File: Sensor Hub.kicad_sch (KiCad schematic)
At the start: 37 parts, among them J1 SWD, J2 SD_Card, J4 USB_B_Micro, SW1 SW_SPDT, SW2 SW_Push, U1 LM20BIM7, U2 STM32L100RBT6A_LQFP64, U3 LD_SSOP, U5 AM2320, U7 APDS-9960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

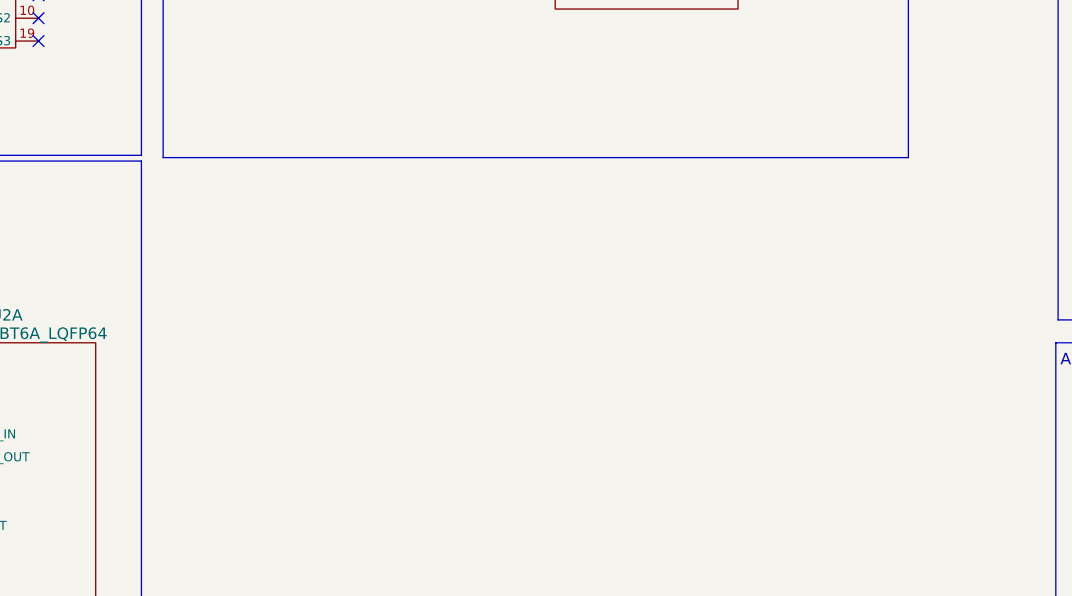
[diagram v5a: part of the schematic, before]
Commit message: Updated Rev 2.0
+ Revamped board to 4 layer with components on both signal layers (top/bottom)
+ Adjusted compactness of components, reducing size by approx 30%
+ Added mounting holes for mounting purposes
- Removed battery, batt charger, eFuse (USB driven only)
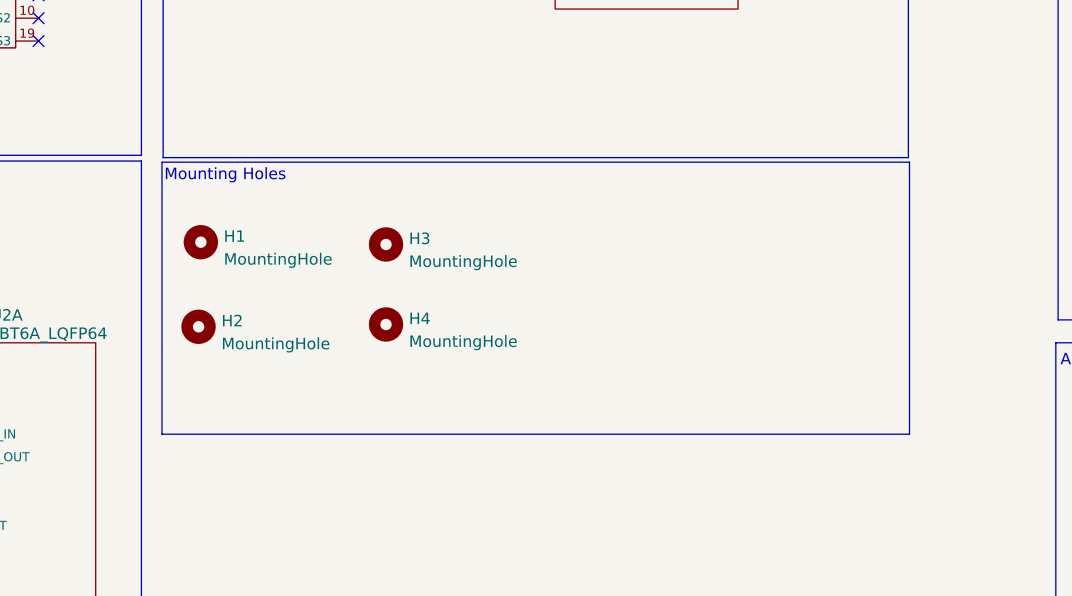
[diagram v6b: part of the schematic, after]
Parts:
- added H1, H2, H3, H4: MountingHole, MountingHole:MountingHole_2.5mm_Pad_Via, symbol Mechanical:MountingHole
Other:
- note added: "Mounting Holes"
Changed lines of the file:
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@@
     (title "Sensor Hub")
     (date "2023-04-03")
-    (rev "1.1")
+    (rev "2.0")
   )
   (junction (at 244.856 82.55) (diameter 0) (color 0 0 0 0)
@@
     (fill (type none))
   )
+  (rectangle (start 103.886 81.534) (end 186.944 111.76)
+    (stroke (width 0) (type default))
+    (fill (type none))
+  )
   (rectangle (start 203.454 60.706) (end 284.48 99.06)
     (stroke (width 0) (type default))
@@
   (text "CLoad = 2* (CL - Cstray)\n" (at 13.716 91.44 0)
     (effects (font (size 1.27 1.27)) (justify left bottom))
+  )
+  (text "Mounting Holes" (at 104.14 83.82 0)
+    (effects (font (size 1.27 1.27) (color 255 39 72 1)) (justify left bottom))
   )
   (text "Ambient Temperature Sensor" (at 203.708 104.394 0)
@@
     )
   )
+  (symbol (lib_id "Mechanical:MountingHole") (at 128.778 90.678 0) (unit 1)
+    (in_bom yes) (on_board yes) (dnp no) (fields_autoplaced)
+    (property "Reference" "H3" (at 131.318 90.043 0)
+      (effects (font (size 1.27 1.27)) (justify left))
+    )
+    (property "Value" "MountingHole" (at 131.318 92.583 0)
+      (effects (font (size 1.27 1.27)) (justify left))
+    )
+    (property "Footprint" "MountingHole:MountingHole_2.5mm_Pad_Via" (at 128.778 90.678 0)
+      (effects (font (size 1.27 1.27)) hide)
+    )
+    (property "Datasheet" "~" (at 128.778 90.678 0)
+      (effects (font (size 1.27 1.27)) hide)
+    )
+    (instances
+      (project "Sensor Hub"
+        (path "/c4cdbb0f-2866-4a3f-8578-00adb185b068"
+          (reference "H3") (unit 1)
+        )
+      )
+    )
+  )
   (symbol (lib_id "power:GND") (at 35.56 97.79 0) (unit 1)
     (in_bom yes) (on_board yes) (dnp no) (fields_autoplaced)
@@
         (path "/c4cdbb0f-2866-4a3f-8578-00adb185b068"
           (reference "R6") (unit 1)
+        )
+      )
+    )
+  )
+  (symbol (lib_id "Mechanical:MountingHole") (at 108.204 90.424 0) (unit 1)
+    (in_bom yes) (on_board yes) (dnp no) (fields_autoplaced)
+    (property "Reference" "H1" (at 110.744 89.789 0)
+      (effects (font (size 1.27 1.27)) (justify left))
+    )
+    (property "Value" "MountingHole" (at 110.744 92.329 0)
+      (effects (font (size 1.27 1.27)) (justify left))
+    )
+    (property "Footprint" "MountingHole:MountingHole_2.5mm_Pad_Via" (at 108.204 90.424 0)
+      (effects (font (size 1.27 1.27)) hide)
+    )
+    (property "Datasheet" "~" (at 108.204 90.424 0)
+      (effects (font (size 1.27 1.27)) hide)
+    )
+    (instances
+      (project "Sensor Hub"
+        (path "/c4cdbb0f-2866-4a3f-8578-00adb185b068"
+          (reference "H1") (unit 1)
         )
       )
@@
         (path "/c4cdbb0f-2866-4a3f-8578-00adb185b068"
           (reference "#PWR012") (unit 1)
+        )
+      )
+    )
+  )
+  (symbol (lib_id "Mechanical:MountingHole") (at 107.95 99.822 0) (unit 1)
+    (in_bom yes) (on_board yes) (dnp no) (fields_autoplaced)
+    (property "Reference" "H2" (at 110.49 99.187 0)
+      (effects (font (size 1.27 1.27)) (justify left))
+    )
+    (property "Value" "MountingHole" (at 110.49 101.727 0)
+      (effects (font (size 1.27 1.27)) (justify left))
+    )
+    (property "Footprint" "MountingHole:MountingHole_2.5mm_Pad_Via" (at 107.95 99.822 0)
+      (effects (font (size 1.27 1.27)) hide)
+    )
+    (property "Datasheet" "~" (at 107.95 99.822 0)
+      (effects (font (size 1.27 1.27)) hide)
+    )
+    (instances
+      (project "Sensor Hub"
+        (path "/c4cdbb0f-2866-4a3f-8578-00adb185b068"
+          (reference "H2") (unit 1)
         )
       )
@@
         )
       )
+    )
+  )
+  (symbol (lib_id "Mechanical:MountingHole") (at 128.778 99.568 0) (unit 1)
+    (in_bom yes) (on_board yes) (dnp no) (fields_autoplaced)
+    (property "Reference" "H4" (at 131.318 98.933 0)
+      (effects (font (size 1.27 1.27)) (justify left))
+    )
+    (property "Value" "MountingHole" (at 131.318 101.473 0)
+      (effects (font (size 1.27 1.27)) (justify left))
+    )
+    (property "Footprint" "MountingHole:MountingHole_2.5mm_Pad_Via" (at 128.778 99.568 0)
+      (effects (font (size 1.27 1.27)) hide)
+    )
+    (property "Datasheet" "~" (at 128.778 99.568 0)
+      (effects (font (size 1.27 1.27)) hide)
+    )
+    (instances
+      (project "Sensor Hub"
+        (path "/c4cdbb0f-2866-4a3f-8578-00adb185b068"
+          (reference "H4") (unit 1)
+        )
+      )

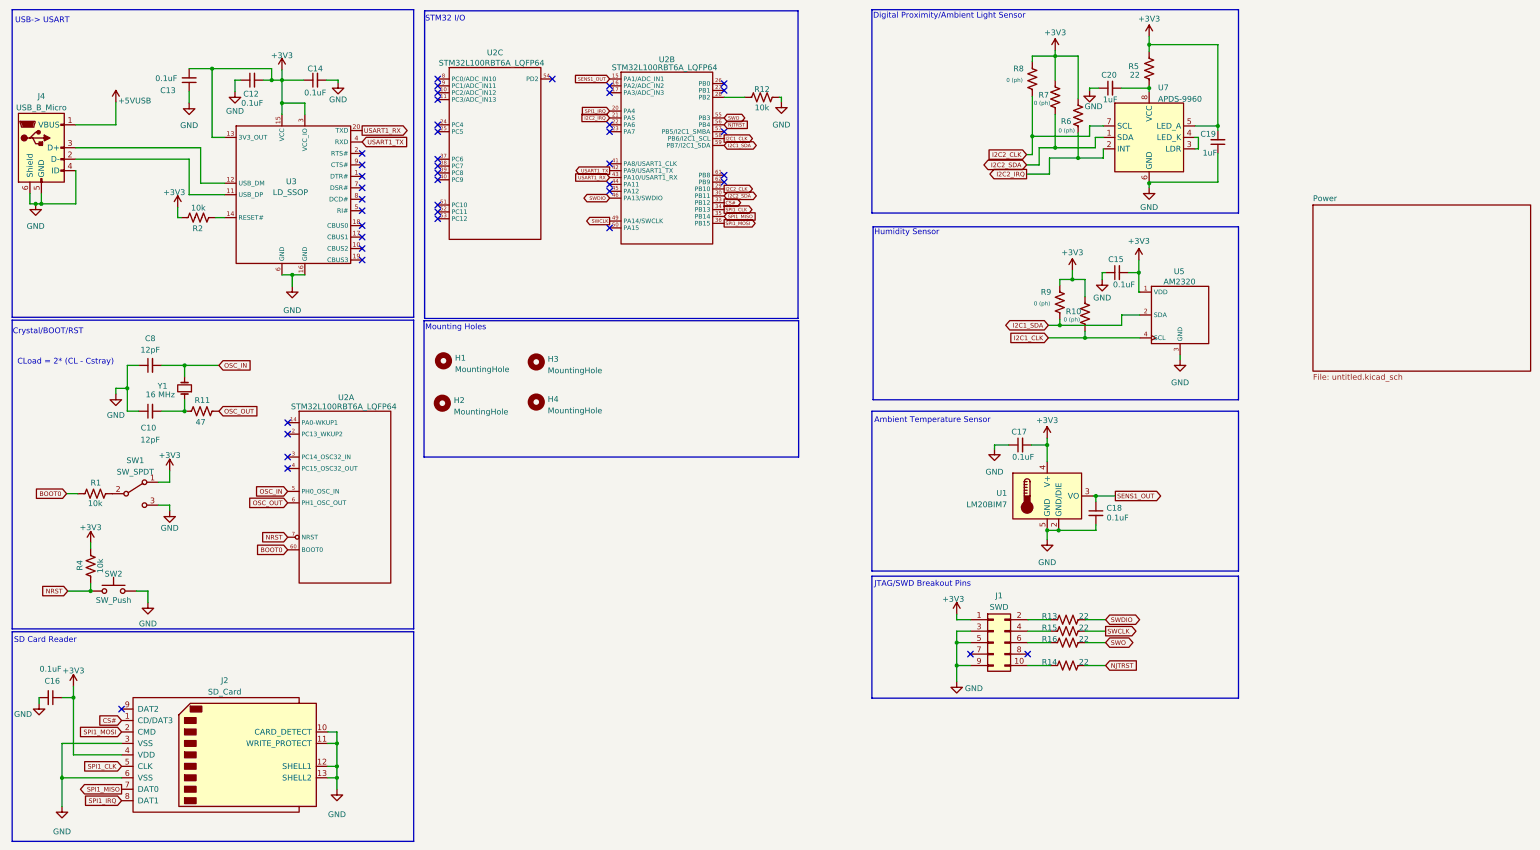
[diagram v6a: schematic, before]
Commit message: Updated to Rev B
+ Added ESD protection on USB side
+ Redesigned board layout to a SIG/GND/GND/SIG stack up and using L4 as 3V3 plane
+ Resized capacitors and resistors to 0402
+ Added 3D models of certain components
+ Added ferrite bead to 5V line
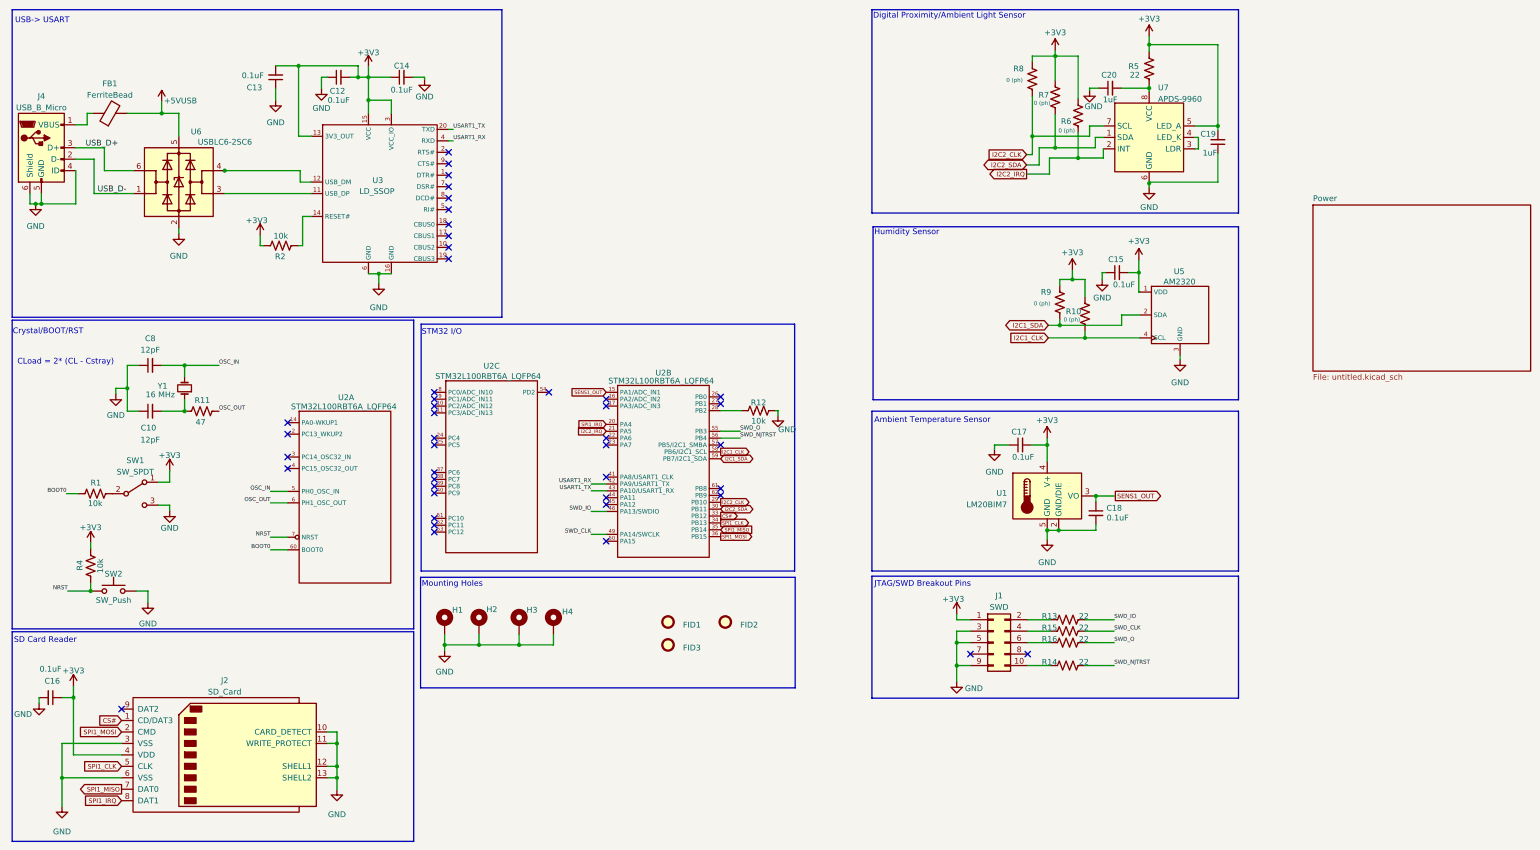
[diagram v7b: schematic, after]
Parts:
- removed H1, H2, H3, H4: MountingHole, MountingHole:MountingHole_2.5mm_Pad_Via, symbol Mechanical:MountingHole
- added FB1: FerriteBead, Ferrite_THT:LairdTech_28C0236-0JW-10, symbol Device:FerriteBead
- added FID1, FID2, FID3: Fiducial, Fiducial:Fiducial_1mm_Mask2mm, symbol Mechanical:Fiducial
- added H1, H2, H3, H4: MountingHole_Pad, MountingHole:MountingHole_2.2mm_M2_Pad_Via, symbol Mechanical:MountingHole_Pad
- added U6: USBLC6-2SC6, Package_TO_SOT_SMD:SOT-23-6, symbol Power_Protection:USBLC6-2SC6
- C10, C8: footprint Capacitor_SMD:C_0805_2012Metric -> Capacitor_SMD:C_0402_1005Metric
- C12, C13, C14, C15, C16, C17, C18, C19, C20: footprint Capacitor_SMD:C_0805_2012Metric -> Capacitor_SMD:C_0603_1608Metric
- R1, R10, R11, R12, R13, R14, R15, R16, R2, R4, R5, R6, R7, R8, R9: footprint Resistor_SMD:R_0805_2012Metric -> Resistor_SMD:R_0402_1005Metric
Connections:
- net +5V: now also FB1.2, U6.5 (VBUS); no longer J4.1 (VBUS)
- net GND: now also H1.1, H2.1, H3.1, H4.1, U6.2 (GND)
- net USART1_RX: now also U2.42 (PA9/USART1_TX), U3.4 (RXD); no longer U2.43 (PA10/USART1_RX), U3.20 (TXD)
- net USART1_TX: now also U2.43 (PA10/USART1_RX), U3.20 (TXD); no longer U2.42 (PA9/USART1_TX), U3.4 (RXD)
- net at U3.11 (USB_DP): now also U6.3 (I/O2); no longer J4.2 (D-)
- net at U3.12 (USB_DM): now also U6.4 (I/O2); no longer J4.3 (D+)
- net NJTRST renamed SWD_NJTRST
- net SWCLK renamed SWD_CLK
- net SWDIO renamed SWD_IO
- net SWO renamed SWD_O
- new net: FB1.1, J4.1 (VBUS)
- new net USB_D+: J4.3 (D+), U6.6 (I/O1)
- new net USB_D-: J4.2 (D-), U6.1 (I/O1)
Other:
- moved on the sheet: C12, C13, C14, R12, R2, U2B, U2C, U3
